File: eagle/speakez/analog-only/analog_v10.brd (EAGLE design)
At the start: 34.5 x 43.2 mm, 22 parts, among them U1 +12v

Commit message: added volume control
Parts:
- added C10: 1uF, SparkFun-Passives:0805
- added C6, C7: 0.1uF, SparkFun-Passives:0805
- added D1, D2, D3, D4, D5, D6: (no value), SparkFun-LED:LED-1206
- added U2: MAX5486, MAX5486:TSSOP24
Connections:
- new net BIAS: U2.11, U2.16, U2.9
- new net HEADPH_L: U2.15
- new net HEADPH_R: U2.10
- new net N$10: D5.C, U2.18
- new net N$11: D6.C, U2.23
- new net N$12: C10.2, U2.12
- new net N$5: D1.C, U2.22
- new net N$6: D2.C, U2.21
- new net N$8: D3.C, U2.20
- new net N$9: D4.C, U2.19
- new net NO_DN: U2.2
- new net NO_MUTE: U2.4
- new net NO_UP: U2.3
- new net RADIO_L: U2.17
- new net RADIO_R: U2.8
- net GND: now also C10.1, C6.2, C7.1, U2.14, U2.24
- net VCC: now also C6.1, C7.2, D1.A, D2.A, D3.A, D4.A, D5.A, D6.A, U2.1, U2.13, U2.6
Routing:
- net VBAT: track 3.33 -> 2.50 mm
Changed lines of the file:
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@@
 <element name="RADIO" library="35mm_audio" package="35MM_SMD_4WIRE" value="SJ-43514-SMT" x="31.75" y="2.54" rot="R90"/>
 <element name="VD2" library="diode" package="SOD123" value="" x="12.7" y="24.384" rot="R90"/>
+<element name="U2" library="MAX5486" package="TSSOP24" value="MAX5486" x="19.685" y="33.02" rot="R90"/>
+<element name="C6" library="SparkFun-Passives" package="0805" value="0.1uF" x="15.24" y="34.29" rot="R90"/>
+<element name="C7" library="SparkFun-Passives" package="0805" value="0.1uF" x="22.86" y="27.305" rot="R270"/>
+<element name="D1" library="SparkFun-LED" package="LED-1206" value="" x="-1.905" y="-19.05"/>
+<element name="D2" library="SparkFun-LED" package="LED-1206" value="" x="-1.905" y="-24.13"/>
+<element name="D3" library="SparkFun-LED" package="LED-1206" value="" x="-1.905" y="-29.21"/>
+<element name="D4" library="SparkFun-LED" package="LED-1206" value="" x="-1.905" y="-34.29"/>
+<element name="D5" library="SparkFun-LED" package="LED-1206" value="" x="-1.905" y="-39.37"/>
+<element name="D6" library="SparkFun-LED" package="LED-1206" value="" x="-1.905" y="-44.45"/>
+<element name="C10" library="SparkFun-Passives" package="0805" value="1uF" x="24.13" y="34.29" rot="R270"/>
 </elements>
 <signals>
@@
 <wire x1="13.716" y1="11.673" x2="11.176" y2="11.038" width="0.1524" layer="1"/>
 <wire x1="11.176" y1="11.038" x2="11.176" y2="10.922" width="0.127" layer="1"/>
-<via x="15.24" y="31.75" extent="1-16" drill="1.27" shape="square"/>
+<via x="13.97" y="31.75" extent="1-16" drill="1.27" shape="square"/>
 <via x="19.05" y="6.35" extent="1-16" drill="1.016"/>
 <via x="19.05" y="3.81" extent="1-16" drill="1.016"/>
@@
 <wire x1="9.525" y1="8.52" x2="9.144" y2="8.139" width="0.1524" layer="1"/>
 <wire x1="6.361" y1="3.175" x2="7.62" y2="3.175" width="0.1524" layer="1"/>
+<contactref element="U2" pad="24"/>
+<contactref element="U2" pad="14"/>
+<contactref element="C7" pad="1"/>
+<contactref element="C6" pad="2"/>
+<contactref element="C10" pad="1"/>
+<wire x1="25.4" y1="36.83" x2="24.13" y2="35.19" width="0" layer="19" extent="1-1"/>
+<wire x1="16.7672" y1="29.445" x2="13.97" y2="31.75" width="0" layer="19" extent="1-1"/>
+<wire x1="15.24" y1="35.19" x2="13.97" y2="31.75" width="0" layer="19" extent="1-1"/>
+<wire x1="16.7672" y1="35.945" x2="15.24" y2="35.19" width="0" layer="19" extent="1-1"/>
+<wire x1="22.86" y1="28.205" x2="16.7672" y2="29.445" width="0" layer="19" extent="1-1"/>
 </signal>
 <signal name="VCC">
@@
 <wire x1="19.05" y1="8.89" x2="15.24" y2="8.89" width="0.1524" layer="16"/>
 <wire x1="15.24" y1="8.89" x2="13.335" y2="6.985" width="0.1524" layer="16"/>
+<contactref element="U2" pad="1"/>
+<contactref element="C6" pad="1"/>
+<contactref element="U2" pad="13"/>
+<contactref element="C7" pad="2"/>
+<contactref element="U2" pad="6"/>
+<contactref element="D6" pad="A"/>
+<contactref element="D5" pad="A"/>
+<contactref element="D4" pad="A"/>
+<contactref element="D3" pad="A"/>
+<contactref element="D2" pad="A"/>
+<contactref element="D1" pad="A"/>
+<wire x1="15.24" y1="33.39" x2="16.7672" y2="36.595" width="0" layer="19" extent="1-1"/>
+<wire x1="22.6028" y1="32.695" x2="16.7672" y2="36.595" width="0" layer="19" extent="1-1"/>
+<wire x1="22.6028" y1="29.445" x2="22.6028" y2="32.695" width="0" layer="19" extent="1-1"/>
+<wire x1="22.86" y1="26.405" x2="22.6028" y2="29.445" width="0" layer="19" extent="1-1"/>
+<wire x1="20.436" y1="24.638" x2="22.86" y2="26.405" width="0" layer="19" extent="1-1"/>
+<wire x1="-3.405" y1="-19.05" x2="4.561" y2="3.175" width="0" layer="19" extent="1-1"/>
+<wire x1="-3.405" y1="-24.13" x2="-3.405" y2="-19.05" width="0" layer="19" extent="1-1"/>
+<wire x1="-3.405" y1="-29.21" x2="-3.405" y2="-24.13" width="0" layer="19" extent="1-1"/>
+<wire x1="-3.405" y1="-34.29" x2="-3.405" y2="-29.21" width="0" layer="19" extent="1-1"/>
+<wire x1="-3.405" y1="-39.37" x2="-3.405" y2="-34.29" width="0" layer="19" extent="1-1"/>
+<wire x1="-3.405" y1="-44.45" x2="-3.405" y2="-39.37" width="0" layer="19" extent="1-1"/>
 </signal>
 <signal name="CLK">
@@
 </signal>
 <signal name="VBAT">
-<via x="15.24" y="28.448" extent="1-16" drill="1.27" shape="square"/>
+<via x="13.97" y="28.448" extent="1-16" drill="1.27" shape="square"/>
 <contactref element="VD2" pad="A"/>
-<wire x1="15.24" y1="28.448" x2="12.7" y2="26.289" width="1.27" layer="1"/>
+<wire x1="13.97" y1="28.448" x2="12.7" y2="26.289" width="1.27" layer="1"/>
 </signal>
 <signal name="VBATSAFE">
@@
 <via x="11.43" y="3.81" extent="1-16" drill="1.016"/>
 </signal>
+<signal name="N$5">
+<contactref element="U2" pad="22"/>
+<contactref element="D1" pad="C"/>
+<wire x1="-0.405" y1="-19.05" x2="16.7672" y2="30.745" width="0" layer="19" extent="1-1"/>
+</signal>
+<signal name="N$6">
+<contactref element="U2" pad="21"/>
+<contactref element="D2" pad="C"/>
+<wire x1="-0.405" y1="-24.13" x2="16.7672" y2="31.395" width="0" layer="19" extent="1-1"/>
+</signal>
+<signal name="N$8">
+<contactref element="U2" pad="20"/>
+<contactref element="D3" pad="C"/>
+<wire x1="-0.405" y1="-29.21" x2="16.7672" y2="32.045" width="0" layer="19" extent="1-1"/>
+</signal>
+<signal name="N$9">
+<contactref element="U2" pad="19"/>
+<contactref element="D4" pad="C"/>
+<wire x1="-0.405" y1="-34.29" x2="16.7672" y2="32.695" width="0" layer="19" extent="1-1"/>
+</signal>
+<signal name="N$10">
+<contactref element="U2" pad="18"/>
+<contactref element="D5" pad="C"/>
+<wire x1="-0.405" y1="-39.37" x2="16.7672" y2="33.345" width="0" layer="19" extent="1-1"/>
+</signal>
+<signal name="N$11">
+<contactref element="U2" pad="23"/>
+<contactref element="D6" pad="C"/>
+<wire x1="-0.405" y1="-44.45" x2="16.7672" y2="30.095" width="0" layer="19" extent="1-1"/>
+</signal>
+<signal name="N$12">
+<contactref element="U2" pad="12"/>
+<contactref element="C10" pad="2"/>
+<wire x1="24.13" y1="33.39" x2="22.6028" y2="36.595" width="0" layer="19" extent="1-1"/>
+</signal>
+<signal name="BIAS">
+<contactref element="U2" pad="9"/>
+<contactref element="U2" pad="11"/>
+<contactref element="U2" pad="16"/>
+<wire x1="22.6028" y1="34.645" x2="22.6028" y2="35.945" width="0" layer="19" extent="1-1"/>
+<wire x1="16.7672" y1="34.645" x2="22.6028" y2="34.645" width="0" layer="19" extent="1-1"/>
+</signal>
+<signal name="RADIO_R">
+<contactref element="U2" pad="8"/>
+</signal>
+<signal name="RADIO_L">
+<contactref element="U2" pad="17"/>
+</signal>
+<signal name="NO_DN">
+<contactref element="U2" pad="2"/>
+</signal>
+<signal name="NO_UP">
+<contactref element="U2" pad="3"/>
+</signal>
+<signal name="NO_MUTE">
+<contactref element="U2" pad="4"/>
+</signal>
+<signal name="HEADPH_L">
+<contactref element="U2" pad="15"/>
+</signal>
+<signal name="HEADPH_R">
+<contactref element="U2" pad="10"/>
+</signal>
 </signals>

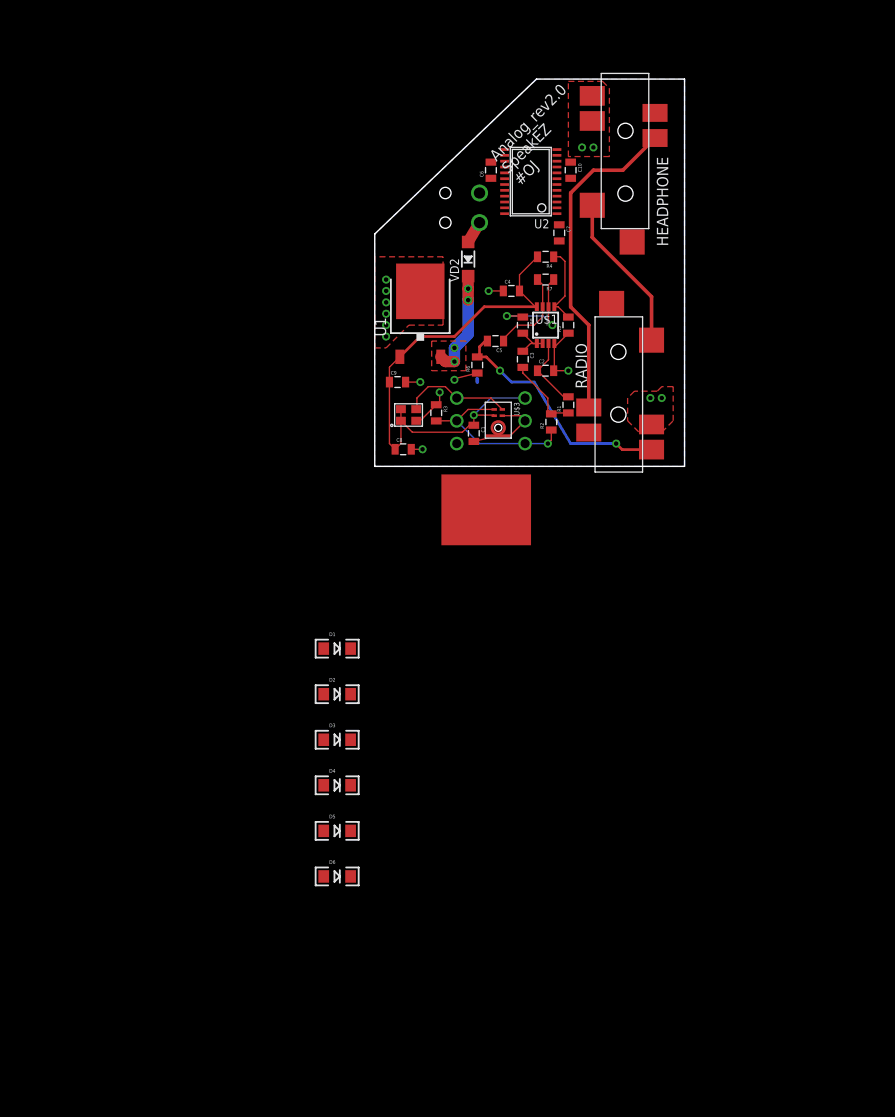
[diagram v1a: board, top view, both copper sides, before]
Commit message: got rid of LED, now resistors
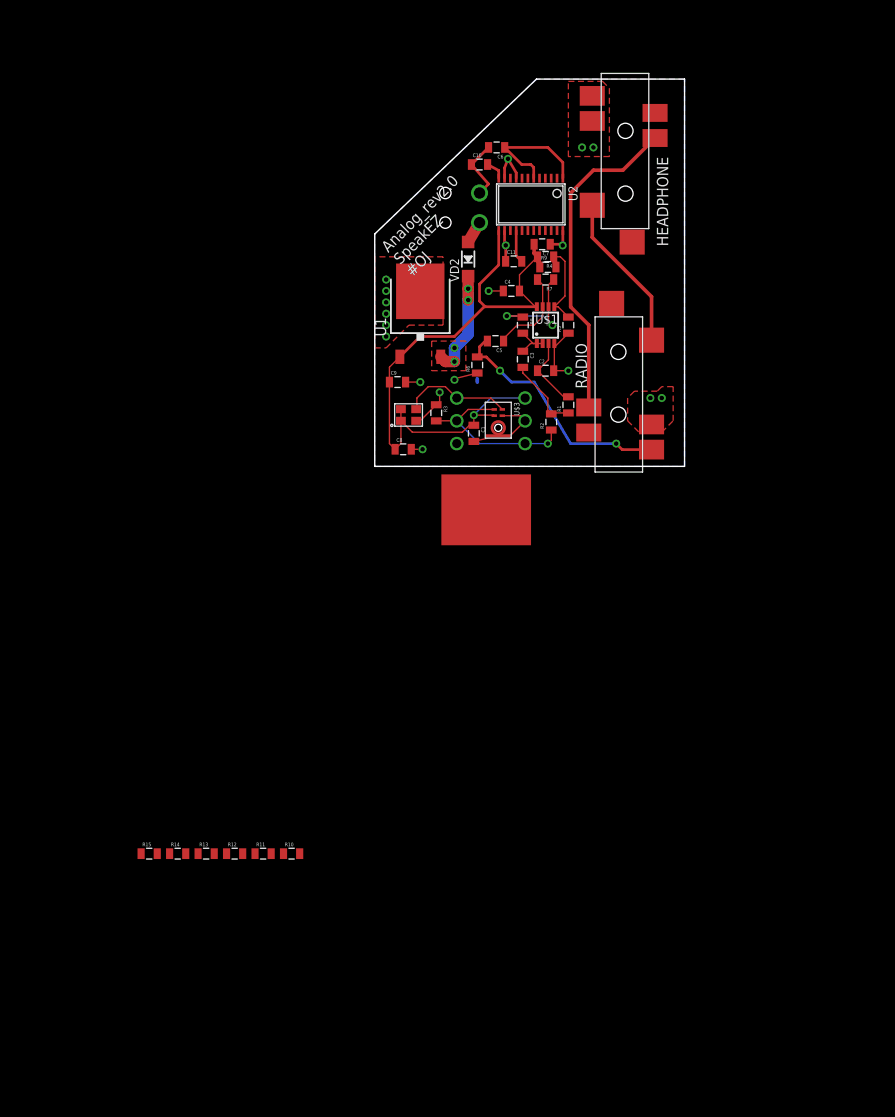
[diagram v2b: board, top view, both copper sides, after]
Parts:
- removed D1, D2, D3, D4, D5, D6: (no value), SparkFun-LED:LED-1206
- added C11: 100pF, SparkFun-Passives:0805
- added R10, R11, R12, R13, R14, R15: 330, SparkFun-Passives:0805
- added R9: 100M, SparkFun-Passives:0805
- moved C10 10.2 mm to (14.0, 34.9), turned to 0 degrees
- moved C6 2.62 mm to (15.9, 36.8), turned to 180 degrees
- moved U2 2.54 mm to (19.7, 30.5), turned to 180 degrees
- moved C7 2.29 mm to (21.0, 26.0), turned to 180 degrees
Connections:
- removed net N$10: D5.C, U2.18
- removed net RADIO_L: U2.17
- removed net RADIO_R: U2.8
- new net N$13: R14.1, R9.2, U2.22
- net BIAS: now also C11.2
- net GND: now also C11.1
- net LEFT: now also U2.17
- net N$11: now also R15.1; no longer D6.C
- net N$5: now also R10.1, U2.18; no longer D1.C, U2.22
- net N$6: now also R11.1, U2.19; no longer D2.C, U2.21
- net N$8: now also R12.1; no longer D3.C
- net N$9: now also R13.1, U2.21; no longer D4.C, U2.19
- net RIGHT: now also U2.8
- net VCC: now also R10.2, R11.2, R12.2, R13.2, R14.2, R15.2, R9.1; no longer D1.A, D2.A, D3.A, D4.A, D5.A, D6.A
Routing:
- net VCC: track 59.4 -> 84.9 mm
- net GND: track 28.3 -> 41.9 mm, vias 19 -> 21
- net BIAS: track 0.00 -> 8.33 mm, vias 0 -> 1
- net N$12: track 0.00 -> 2.27 mm

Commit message: added zero ohm resistors...just couldn't resist
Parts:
- added C12, C13, C14, C15: 0.1 uF, SparkFun-Passives:0805
- added R16, R17, R21, R22: 1k, SparkFun-Passives:0805
- added R18, R23: 100k, SparkFun-Resistors:0805
- added R19, R20, R24, R25: 1k, SparkFun-Resistors:0805
- added R26, R27: 0, SparkFun-Passives:0805
- added U$4: MCP6L92, Microchip_By_element14_Batch_1:MSOP8
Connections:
- new net HP_L_AMPD: C15.2, R23.2, R26.1
- new net HP_R_AMPD: C13.2, R18.2, R27.1
- new net N$10: R19.1, R20.1, U$4.6
- new net N$14: R24.1, R25.1, U$4.3
- net GND: now also C12.1, C14.1, R17.1, R18.1, R22.1, R23.1
- net HEADPH_L: now also R25.2
- net HEADPH_R: now also R20.2
- net LEFT: now also R26.2
- net VCC: now also C12.2, C14.2, R16.2, R21.2, U$4.1, U$4.8
- net VIRT_GND: now also R16.1, R17.2, R21.1, R22.2, U$4.4, U$4.5
- net VOUT_AMP: now also C13.1, C15.1, R19.2, R24.2, U$4.2, U$4.7
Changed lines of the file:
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@@
 <element name="R14" library="SparkFun-Passives" package="0805" value="330" x="-19.685" y="-41.91"/>
 <element name="R15" library="SparkFun-Passives" package="0805" value="330" x="-22.86" y="-41.91"/>
+<element name="U$4" library="Microchip_By_element14_Batch_1" package="MSOP8" value="MCP6L92" x="-29.845" y="-40.005"/>
+<element name="C12" library="SparkFun-Passives" package="0805" value="0.1 uF" x="-29.845" y="-50.8"/>
+<element name="R16" library="SparkFun-Passives" package="0805" value="1k" x="-23.495" y="-50.8"/>
+<element name="R17" library="SparkFun-Passives" package="0805" value="1k" x="-29.845" y="-55.245"/>
+<element name="C13" library="SparkFun-Passives" package="0805" value="0.1 uF" x="-26.67" y="-50.8"/>
+<element name="R18" library="SparkFun-Resistors" package="0805" value="100k" x="-29.845" y="-46.355"/>
+<element name="R19" library="SparkFun-Resistors" package="0805" value="1k" x="-26.67" y="-46.355"/>
+<element name="R20" library="SparkFun-Resistors" package="0805" value="1k" x="-23.495" y="-46.355"/>
+<element name="C14" library="SparkFun-Passives" package="0805" value="0.1 uF" x="-29.845" y="-64.135"/>
+<element name="R21" library="SparkFun-Passives" package="0805" value="1k" x="-23.495" y="-64.135"/>
+<element name="R22" library="SparkFun-Passives" package="0805" value="1k" x="-29.845" y="-68.58"/>
+<element name="C15" library="SparkFun-Passives" package="0805" value="0.1 uF" x="-26.67" y="-64.135"/>
+<element name="R23" library="SparkFun-Resistors" package="0805" value="100k" x="-29.845" y="-59.69"/>
+<element name="R24" library="SparkFun-Resistors" package="0805" value="1k" x="-26.67" y="-59.69"/>
+<element name="R25" library="SparkFun-Resistors" package="0805" value="1k" x="-23.495" y="-59.69"/>
+<element name="R26" library="SparkFun-Passives" package="0805" value="0" x="-33.02" y="-68.58"/>
+<element name="R27" library="SparkFun-Passives" package="0805" value="0" x="-36.195" y="-68.58"/>
 </elements>
 <signals>
@@
 <wire x1="16.891" y1="25.908" x2="16.891" y2="24.141" width="0.3048" layer="1"/>
 <wire x1="16.891" y1="24.141" x2="16.88" y2="24.13" width="0.3048" layer="1"/>
+<contactref element="C12" pad="1"/>
+<contactref element="R17" pad="1"/>
+<contactref element="R18" pad="1"/>
+<contactref element="C14" pad="1"/>
+<contactref element="R22" pad="1"/>
+<contactref element="R23" pad="1"/>
+<wire x1="-30.745" y1="-64.135" x2="-30.745" y2="-68.58" width="0" layer="19" extent="1-1"/>
+<wire x1="-30.745" y1="-59.69" x2="-30.745" y2="-64.135" width="0" layer="19" extent="1-1"/>
+<wire x1="-30.745" y1="-55.245" x2="-30.745" y2="-59.69" width="0" layer="19" extent="1-1"/>
+<wire x1="-30.745" y1="-50.8" x2="-30.745" y2="-55.245" width="0" layer="19" extent="1-1"/>
+<wire x1="-30.745" y1="-46.355" x2="-30.745" y2="-50.8" width="0" layer="19" extent="1-1"/>
+<wire x1="6.361" y1="3.175" x2="-30.745" y2="-46.355" width="0" layer="19" extent="1-1"/>
 </signal>
 <signal name="VCC">
@@
 <contactref element="R14" pad="2"/>
 <contactref element="R15" pad="2"/>
+<contactref element="C12" pad="2"/>
+<contactref element="R16" pad="2"/>
+<contactref element="C14" pad="2"/>
+<contactref element="R21" pad="2"/>
+<contactref element="U$4" pad="8"/>
+<contactref element="U$4" pad="1"/>
+<wire x1="-22.595" y1="-64.135" x2="-28.945" y2="-64.135" width="0" layer="19" extent="1-1"/>
+<wire x1="-28.945" y1="-50.8" x2="-28.945" y2="-64.135" width="0" layer="19" extent="1-1"/>
+<wire x1="-22.595" y1="-50.8" x2="-28.945" y2="-50.8" width="0" layer="19" extent="1-1"/>
+<wire x1="-21.96" y1="-41.91" x2="-22.595" y2="-50.8" width="0" layer="19" extent="1-1"/>
 <wire x1="-18.785" y1="-41.91" x2="-21.96" y2="-41.91" width="0" layer="19" extent="1-1"/>
 <wire x1="-15.61" y1="-41.91" x2="-18.785" y2="-41.91" width="0" layer="19" extent="1-1"/>
@@
 <wire x1="-9.26" y1="-41.91" x2="-12.435" y2="-41.91" width="0" layer="19" extent="1-1"/>
 <wire x1="-6.085" y1="-41.91" x2="-9.26" y2="-41.91" width="0" layer="19" extent="1-1"/>
+<wire x1="-30.82" y1="-42.055" x2="-21.96" y2="-41.91" width="0" layer="19" extent="1-1"/>
+<wire x1="-30.82" y1="-37.955" x2="-30.82" y2="-42.055" width="0" layer="19" extent="1-1"/>
 <wire x1="4.561" y1="3.175" x2="-6.085" y2="-41.91" width="0" layer="19" extent="1-1"/>
 <wire x1="20.69" y1="23.495" x2="20.436" y2="24.638" width="0" layer="19" extent="1-1"/>
@@
 <wire x1="23.495" y1="24.13" x2="23.495" y2="20.252" width="0.1524" layer="1"/>
 <wire x1="23.495" y1="20.252" x2="22.311" y2="19.068" width="0.1524" layer="1"/>
+<contactref element="R16" pad="1"/>
+<contactref element="R17" pad="2"/>
+<contactref element="R21" pad="1"/>
+<contactref element="R22" pad="2"/>
+<contactref element="U$4" pad="5"/>
+<contactref element="U$4" pad="4"/>
+<wire x1="-24.395" y1="-64.135" x2="-28.945" y2="-68.58" width="0" layer="19" extent="1-1"/>
+<wire x1="-28.945" y1="-55.245" x2="-24.395" y2="-64.135" width="0" layer="19" extent="1-1"/>
+<wire x1="-24.395" y1="-50.8" x2="-28.945" y2="-55.245" width="0" layer="19" extent="1-1"/>
+<wire x1="-28.87" y1="-42.055" x2="-24.395" y2="-50.8" width="0" layer="19" extent="1-1"/>
+<wire x1="-28.87" y1="-37.955" x2="-28.87" y2="-42.055" width="0" layer="19" extent="1-1"/>
+<wire x1="22.311" y1="19.068" x2="-28.87" y2="-37.955" width="0" layer="19" extent="1-1"/>
 </signal>
 <signal name="AUDIO_AMPD">
@@
 <wire x1="20.066" y1="17.018" x2="21.011" y2="17.963" width="0.1524" layer="1"/>
 <wire x1="21.011" y1="17.963" x2="21.011" y2="19.068" width="0.1524" layer="1"/>
+<contactref element="C13" pad="1"/>
+<contactref element="R19" pad="2"/>
+<contactref element="C15" pad="1"/>
+<contactref element="R24" pad="2"/>
+<contactref element="U$4" pad="7"/>
+<contactref element="U$4" pad="2"/>
+<wire x1="-25.77" y1="-59.69" x2="-27.57" y2="-64.135" width="0" layer="19" extent="1-1"/>
+<wire x1="-27.57" y1="-50.8" x2="-25.77" y2="-59.69" width="0" layer="19" extent="1-1"/>
+<wire x1="-25.77" y1="-46.355" x2="-27.57" y2="-50.8" width="0" layer="19" extent="1-1"/>
+<wire x1="-30.17" y1="-42.055" x2="-25.77" y2="-46.355" width="0" layer="19" extent="1-1"/>
+<wire x1="-30.17" y1="-37.955" x2="-30.17" y2="-42.055" width="0" layer="19" extent="1-1"/>
+<wire x1="16.648" y1="15.24" x2="-30.17" y2="-37.955" width="0" layer="19" extent="1-1"/>
 </signal>
 <signal name="N$7">
@@
 <wire x1="26.54" y1="26.8" x2="26.54" y2="30.38" width="0.4064" layer="1"/>
 <contactref element="U2" pad="17"/>
+<contactref element="R26" pad="2"/>
+<wire x1="33.15" y1="15.34" x2="-32.12" y2="-68.58" width="0" layer="19" extent="1-1"/>
 <wire x1="18.71" y1="27.5622" x2="26.54" y2="26.8" width="0" layer="19" extent="1-1"/>
 </signal>
@@
 <signal name="HEADPH_L">
 <contactref element="U2" pad="15"/>
+<contactref element="R25" pad="2"/>
+<wire x1="17.41" y1="27.5622" x2="-22.595" y2="-59.69" width="0" layer="19" extent="1-1"/>
 </signal>
 <signal name="HEADPH_R">
 <contactref element="U2" pad="10"/>
+<contactref element="R20" pad="2"/>
+<wire x1="17.41" y1="33.3978" x2="-22.595" y2="-46.355" width="0" layer="19" extent="1-1"/>
 </signal>
 <signal name="N$13">
@@
 <wire x1="22.61" y1="27.5622" x2="-23.76" y2="-41.91" width="0" layer="19" extent="1-1"/>
 </signal>
+<signal name="N$10">
+<contactref element="R19" pad="1"/>
+<contactref element="R20" pad="1"/>
+<contactref element="U$4" pad="6"/>
+<wire x1="-24.395" y1="-46.355" x2="-27.57" y2="-46.355" width="0" layer="19" extent="1-1"/>
+<wire x1="-29.52" y1="-37.955" x2="-27.57" y2="-46.355" width="0" layer="19" extent="1-1"/>
+</signal>
+<signal name="N$14">
+<contactref element="R24" pad="1"/>
+<contactref element="R25" pad="1"/>
+<contactref element="U$4" pad="3"/>
+<wire x1="-24.395" y1="-59.69" x2="-27.57" y2="-59.69" width="0" layer="19" extent="1-1"/>
+<wire x1="-29.52" y1="-42.055" x2="-27.57" y2="-59.69" width="0" layer="19" extent="1-1"/>
+</signal>
+<signal name="HP_R_AMPD">
+<contactref element="C13" pad="2"/>
+<contactref element="R18" pad="2"/>
+<contactref element="R27" pad="1"/>
+<wire x1="-25.77" y1="-50.8" x2="-37.095" y2="-68.58" width="0" layer="19" extent="1-1"/>
+<wire x1="-28.945" y1="-46.355" x2="-25.77" y2="-50.8" width="0" layer="19" extent="1-1"/>
+</signal>
+<signal name="HP_L_AMPD">
+<contactref element="C15" pad="2"/>
+<contactref element="R23" pad="2"/>
+<contactref element="R26" pad="1"/>
+<wire x1="-25.77" y1="-64.135" x2="-33.92" y2="-68.58" width="0" layer="19" extent="1-1"/>
+<wire x1="-28.945" y1="-59.69" x2="-25.77" y2="-64.135" width="0" layer="19" extent="1-1"/>
+</signal>
 </signals>
